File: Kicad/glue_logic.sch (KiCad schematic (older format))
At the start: 14 parts, among them U12 SN74LS273, U13 DM74AS74M, U14 DM74AS74M, U15 74AS04, U16 DM74S05M, U17 74F151A, U18 DM74AS74M, U19 74F151A, U37 DM74AS74M, U49 SN74AS258, U5 DM74S05M, U50 SN74AS258, U51 DM74AS74M, U7 DM74AS74M

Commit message: few glued wires
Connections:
- net labels added: CN4_5, D20, D22, D23, D24, U36_13, U44_1, U46_19, U6_13, U6_16, U6_34, U6_73, _BOSS, _IPL1
- wire segments 204 -> 264
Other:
- moved on the sheet: U12, U37, U5
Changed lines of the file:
@@
 L New_Library_0:DM74AS74M U37
 U 1 1 5DC69234
-P 3400 7050
-F 0 "U37" H 3567 7615 50  0000 C CNN
-F 1 "DM74AS74M" H 3567 7524 50  0000 C CNN
-F 2 "" H 3400 7050 50  0001 C CNN
-F 3 "" H 3400 7050 50  0001 C CNN
-	1    3400 7050
+P 5950 7050
+F 0 "U37" H 6117 7615 50  0000 C CNN
+F 1 "DM74AS74M" H 6117 7524 50  0000 C CNN
+F 2 "" H 5950 7050 50  0001 C CNN
+F 3 "" H 5950 7050 50  0001 C CNN
+	1    5950 7050
 	1    0    0    -1
 $EndComp
@@
 L New_Library_0:DM74S05M U5
 U 1 1 5DC6A3D2
-P 1200 7000
-F 0 "U5" H 1200 7565 50  0000 C CNN
-F 1 "DM74S05M" H 1200 7474 50  0000 C CNN
-F 2 "" H 1200 6800 50  0001 C CNN
-F 3 "" H 1200 6800 50  0001 C CNN
-	1    1200 7000
+P 2550 6700
+F 0 "U5" H 2550 7265 50  0000 C CNN
+F 1 "DM74S05M" H 2550 7174 50  0000 C CNN
+F 2 "" H 2550 6500 50  0001 C CNN
+F 3 "" H 2550 6500 50  0001 C CNN
+	1    2550 6700
 	1    0    0    -1
 $EndComp
@@
 L New_Library_0:SN74LS273 U12
 U 1 1 5DC6B7D4
-P 2250 7000
-F 0 "U12" H 2225 7665 50  0000 C CNN
-F 1 "SN74LS273" H 2225 7574 50  0000 C CNN
-F 2 "" H 2250 7250 50  0001 C CNN
-F 3 "" H 2250 7250 50  0001 C CNN
-	1    2250 7000
+P 8800 5400
+F 0 "U12" H 8775 6065 50  0000 C CNN
+F 1 "SN74LS273" H 8775 5974 50  0000 C CNN
+F 2 "" H 8800 5650 50  0001 C CNN
+F 3 "" H 8800 5650 50  0001 C CNN
+	1    8800 5400
 	1    0    0    -1
 $EndComp
@@
 U3_16
 Wire Wire Line
-	1100 5650 1800 5650
+	1100 5650 1600 5650
 Wire Wire Line
 	1800 5650 1800 5350
@@
 Wire Wire Line
 	2050 4300 2150 4300
-Wire Wire Line
-	1100 4250 2050 4250
 Text GLabel 1100 2850 0    50   Input ~ 0
 U9_10
@@
 	5400 5550 5200 5550
 Wire Wire Line
+	1950 6400 2250 6400
+Wire Wire Line
+	1100 4250 2050 4250
+Text GLabel 1100 6700 0    50   Input ~ 0
+U6_13
+Wire Wire Line
+	2250 6700 1100 6700
+Wire Wire Line
+	2100 5950 2100 6600
+Wire Wire Line
+	2100 6600 2250 6600
+Wire Wire Line
+	2100 5950 5800 5950
+Wire Wire Line
+	5800 5950 5800 2150
+Wire Wire Line
+	5800 2150 5350 2150
+Text GLabel 1100 2150 0    50   Input ~ 0
+U6_34
+Wire Wire Line
+	4550 1650 4300 1650
+Wire Wire Line
+	4300 1650 4300 1000
+Wire Wire Line
+	4300 1000 1250 1000
+Wire Wire Line
+	1250 1000 1250 2150
+Wire Wire Line
+	1250 2150 1100 2150
+Wire Wire Line
+	4550 1850 4450 1850
+Wire Wire Line
+	4450 1850 4450 1400
+$Comp
+L power:+5V #PWR?
+U 1 1 5DA035B7
+P 4450 1400
+F 0 "#PWR?" H 4450 1250 50  0001 C CNN
+F 1 "+5V" H 4465 1573 50  0000 C CNN
+F 2 "" H 4450 1400 50  0001 C CNN
+F 3 "" H 4450 1400 50  0001 C CNN
+	1    4450 1400
+	1    0    0    -1
+$EndComp
+$Comp
+L power:+5V #PWR?
+U 1 1 5DA039F0
+P 5450 1400
+F 0 "#PWR?" H 5450 1250 50  0001 C CNN
+F 1 "+5V" H 5465 1573 50  0000 C CNN
+F 2 "" H 5450 1400 50  0001 C CNN
+F 3 "" H 5450 1400 50  0001 C CNN
+	1    5450 1400
+	1    0    0    -1
+$EndComp
+Wire Wire Line
+	5350 1550 5450 1550
+Wire Wire Line
+	5450 1550 5450 1400
+Wire Wire Line
+	4650 3950 4550 3950
+Wire Wire Line
+	4550 3950 4550 3500
+Wire Wire Line
+	4550 3500 6200 3500
+Wire Wire Line
+	6200 3500 6200 2200
+Wire Wire Line
+	6200 2200 6400 2200
+Text GLabel 6400 2200 2    50   Input ~ 0
+CN4_5
+Text Label 6200 2200 0    50   ~ 0
+_RES
+Wire Wire Line
+	4650 4050 4400 4050
+Wire Wire Line
+	4400 4050 4400 5850
+Wire Wire Line
+	1900 5850 1900 4950
+Wire Wire Line
+	1900 4950 1100 4950
+Wire Wire Line
+	1900 5850 4400 5850
+Text Label 1150 4950 0    50   ~ 0
+_BOSS
+Wire Wire Line
+	5250 4350 6400 4350
+Wire Wire Line
+	5250 4250 5900 4250
+Wire Wire Line
+	5900 4250 5900 2300
+Wire Wire Line
+	5900 2300 6350 2300
+Text GLabel 6400 2300 2    50   Input ~ 0
+U36_13
+Text GLabel 6400 2400 2    50   Input ~ 0
+U44_1
+Wire Wire Line
+	6400 2400 6350 2400
+Wire Wire Line
+	6350 2400 6350 2300
+Connection ~ 6350 2300
+Wire Wire Line
+	6350 2300 6400 2300
+Wire Wire Line
+	6400 3950 6400 3850
+Wire Wire Line
+	6300 3850 6400 3850
+Connection ~ 6400 3850
+Wire Wire Line
+	2250 6800 1600 6800
+Wire Wire Line
+	1600 5650 1600 6800
+Connection ~ 1600 5650
+Wire Wire Line
+	1600 5650 1800 5650
+Wire Wire Line
+	2250 6900 1100 6900
+Text Label 1150 6900 0    50   ~ 0
+_IPL1
+Wire Wire Line
+	7800 5300 7250 5300
+Wire Wire Line
+	7800 5000 8000 5000
+Wire Wire Line
+	7800 5000 7800 5300
+Text GLabel 8000 4750 1    50   Input ~ 0
+U6_73
+Wire Wire Line
+	8000 4750 8000 5000
+Connection ~ 8000 5000
+Wire Wire Line
+	8000 5000 8450 5000
+Text GLabel 8100 4750 1    50   Input ~ 0
+U6_16
+Wire Wire Line
+	8100 4750 8100 5100
+Wire Wire Line
+	8100 5100 8450 5100
+Wire Wire Line
+	8450 5200 8200 5200
+Wire Wire Line
+	8200 5200 8200 4750
+Text GLabel 8200 4750 1    50   Input ~ 0
+U46_19
+Text Label 8200 4800 3    50   ~ 0
+D20
+Wire Wire Line
+	8450 5300 8300 5300
+Wire Wire Line
+	8300 5300 8300 4750
+Text Label 8300 4800 3    50   ~ 0
+D24
+Wire Wire Line
+	8450 5500 8000 5500
+Wire Wire Line
+	8000 5500 8000 6050
+Wire Wire Line
+	8450 5600 8100 5600
+Wire Wire Line
+	8100 5600 8100 6050
+Wire Wire Line
+	8450 5700 8200 5700
+Wire Wire Line
+	8200 5700 8200 6050
+Wire Wire Line
+	8450 5800 8300 5800
+Wire Wire Line
+	8300 5800 8300 6050
+Text Label 8100 5850 3    50   ~ 0
+D22
+Text Label 8200 5850 3    50   ~ 0
+D23
+Wire Wire Line
+	10200 4700 10350 4700
+Wire Wire Line
+	10350 4700 10350 4500
+Wire Wire Line
+	8650 3000 9250 3000
+Wire Wire Line
+	8650 1500 9250 1500
+Wire Wire Line
 	7300 1400 8000 1400
 Wire Wire Line
 	7300 2900 8000 2900
-Wire Wire Line
-	8650 3000 9250 3000
-Wire Wire Line
-	8650 1500 9250 1500
 Wire Bus Line
 	9350 700  9350 3200
@@
 	7200 700  7200 3100
 Wire Bus Line
+	9150 600  9150 3100
+Wire Bus Line
 	7450 600  7450 3000
-Wire Bus Line
-	9150 600  9150 3100
 $EndSCHEMATC

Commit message: nothing special
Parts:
- added R38, R39: 220R, symbol Device:R
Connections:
- net labels added: D16, D17, D18, D19, U11_12, U30_18, U6_58, U6_59, U6_61, U8_35
- wire segments 264 -> 295
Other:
- moved on the sheet: U37
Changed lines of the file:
@@
 L New_Library_0:DM74AS74M U37
 U 1 1 5DC69234
-P 5950 7050
-F 0 "U37" H 6117 7615 50  0000 C CNN
-F 1 "DM74AS74M" H 6117 7524 50  0000 C CNN
-F 2 "" H 5950 7050 50  0001 C CNN
-F 3 "" H 5950 7050 50  0001 C CNN
-	1    5950 7050
+P 4900 6850
+F 0 "U37" H 5067 7415 50  0000 C CNN
+F 1 "DM74AS74M" H 5067 7324 50  0000 C CNN
+F 2 "" H 4900 6850 50  0001 C CNN
+F 3 "" H 4900 6850 50  0001 C CNN
+	1    4900 6850
 	1    0    0    -1
 $EndComp
@@
 	7800 5300 7250 5300
 Wire Wire Line
-	7800 5000 8000 5000
+	7800 5000 7900 5000
 Wire Wire Line
 	7800 5000 7800 5300
-Text GLabel 8000 4750 1    50   Input ~ 0
+Text GLabel 7900 4750 1    50   Input ~ 0
 U6_73
 Wire Wire Line
-	8000 4750 8000 5000
-Connection ~ 8000 5000
-Wire Wire Line
-	8000 5000 8450 5000
-Text GLabel 8100 4750 1    50   Input ~ 0
+	7900 4750 7900 5000
+Connection ~ 7900 5000
+Wire Wire Line
+	7900 5000 8450 5000
+Text GLabel 8300 4750 1    50   Input ~ 0
 U6_16
 Wire Wire Line
-	8100 4750 8100 5100
-Wire Wire Line
-	8100 5100 8450 5100
+	8300 4750 8300 5100
+Wire Wire Line
+	8300 5100 8450 5100
 Wire Wire Line
 	8450 5200 8200 5200
@@
 D20
 Wire Wire Line
-	8450 5300 8300 5300
-Wire Wire Line
-	8300 5300 8300 4750
-Text Label 8300 4800 3    50   ~ 0
+	8450 5300 8100 5300
+Wire Wire Line
+	8100 5300 8100 4750
+Text Label 8100 4800 3    50   ~ 0
 D24
 Wire Wire Line
 	8450 5500 8000 5500
 Wire Wire Line
-	8000 5500 8000 6050
+	8000 5500 8000 5950
 Wire Wire Line
 	8450 5600 8100 5600
@@
 	8450 5800 8300 5800
 Wire Wire Line
-	8300 5800 8300 6050
+	8300 5800 8300 5950
 Text Label 8100 5850 3    50   ~ 0
 D22
@@
 D23
 Wire Wire Line
-	10200 4700 10350 4700
-Wire Wire Line
-	10350 4700 10350 4500
+	9100 5700 9350 5700
+Wire Wire Line
+	9350 5700 9350 6050
+Text Label 9450 5850 3    50   ~ 0
+D17
+Wire Wire Line
+	9100 5600 9450 5600
+Wire Wire Line
+	9450 5600 9450 6050
+Text Label 9350 5850 3    50   ~ 0
+D18
+Wire Wire Line
+	9100 5200 9450 5200
+Wire Wire Line
+	9450 5200 9450 4750
+Text Label 9450 4800 3    50   ~ 0
+D19
+Wire Wire Line
+	9100 5300 9550 5300
+Wire Wire Line
+	9550 5300 9550 4750
+Text Label 9550 4800 3    50   ~ 0
+D16
+Wire Wire Line
+	8450 5400 8000 5400
+Wire Wire Line
+	8000 5400 8000 4750
+Wire Wire Line
+	9100 5900 9200 5900
+Wire Wire Line
+	9200 5900 9200 6250
+Wire Wire Line
+	7800 6250 7800 5500
+Wire Wire Line
+	7800 5500 7250 5500
+Text GLabel 8050 6350 2    50   Input ~ 0
+U30_18
+Wire Wire Line
+	7800 6250 7900 6250
+Wire Wire Line
+	8050 6350 7900 6350
+Wire Wire Line
+	7900 6350 7900 6250
+Connection ~ 7900 6250
+Wire Wire Line
+	7900 6250 9200 6250
+Text GLabel 8000 4750 1    50   Input ~ 0
+U6_61
+Text Label 8000 4800 3    50   ~ 0
+D24
+Text GLabel 8000 5950 3    50   Input ~ 0
+U6_58
+Text Label 8000 5800 3    50   ~ 0
+D22
+Text Label 8300 5850 3    50   ~ 0
+D23
+Text GLabel 8300 5950 3    50   Input ~ 0
+U6_59
+$Comp
+L power:+5V #PWR?
+U 1 1 5DD59290
+P 4450 6400
+F 0 "#PWR?" H 4450 6250 50  0001 C CNN
+F 1 "+5V" H 4465 6573 50  0000 C CNN
+F 2 "" H 4450 6400 50  0001 C CNN
+F 3 "" H 4450 6400 50  0001 C CNN
+	1    4450 6400
+	1    0    0    -1
+$EndComp
+Wire Wire Line
+	5300 6550 5350 6550
+Wire Wire Line
+	5350 6550 5350 6400
+Wire Wire Line
+	5350 6400 4450 6400
+Text GLabel 1100 7150 0    50   Input ~ 0
+U8_35
+Wire Wire Line
+	1100 7150 3450 7150
+Wire Wire Line
+	4450 6400 4450 6550
+Wire Wire Line
+	4450 6550 4500 6550
+Connection ~ 4450 6400
+Wire Wire Line
+	4500 6750 4000 6750
+Wire Wire Line
+	4000 6750 4000 7150
+Wire Wire Line
+	5300 6850 5600 6850
+Wire Wire Line
+	5600 6850 5600 7450
+Wire Wire Line
+	5600 7450 4000 7450
+Wire Wire Line
+	4000 7450 4000 7150
+Connection ~ 4000 7150
+$Comp
+L Device:R R38
+U 1 1 5E5CC419
+P 3450 7000
+F 0 "R38" H 3520 7046 50  0000 L CNN
+F 1 "220R" H 3520 6955 50  0000 L CNN
+F 2 "" V 3380 7000 50  0001 C CNN
+F 3 "~" H 3450 7000 50  0001 C CNN
+	1    3450 7000
+	1    0    0    -1
+$EndComp
+Connection ~ 3450 7150
+Wire Wire Line
+	3450 7150 4000 7150
+$Comp
+L Device:R R39
+U 1 1 5E5CCBD0
+P 3450 7300
+F 0 "R39" H 3520 7346 50  0000 L CNN
+F 1 "220R" H 3520 7255 50  0000 L CNN
+F 2 "" V 3380 7300 50  0001 C CNN
+F 3 "~" H 3450 7300 50  0001 C CNN
+	1    3450 7300
+	1    0    0    -1
+$EndComp
+$Comp
+L power:+5V #PWR?
+U 1 1 5E5CD0AB
+P 3450 6850
+F 0 "#PWR?" H 3450 6700 50  0001 C CNN
+F 1 "+5V" H 3465 7023 50  0000 C CNN
+F 2 "" H 3450 6850 50  0001 C CNN
+F 3 "" H 3450 6850 50  0001 C CNN
+	1    3450 6850
+	1    0    0    -1
+$EndComp
+$Comp
+L power:GND #PWR?
+U 1 1 5E5CD473
+P 3450 7450
+F 0 "#PWR?" H 3450 7200 50  0001 C CNN
+F 1 "GND" H 3455 7277 50  0000 C CNN
+F 2 "" H 3450 7450 50  0001 C CNN
+F 3 "" H 3450 7450 50  0001 C CNN
+	1    3450 7450
+	1    0    0    -1
+$EndComp
+Wire Wire Line
+	4500 6650 4000 6650
+Wire Wire Line
+	4000 6650 4000 6600
 Wire Wire Line
 	8650 3000 9250 3000
@@
 Wire Bus Line
 	7450 600  7450 3000
+Text GLabel 4000 6600 1    50   Input ~ 0
+U11_12
 $EndSCHEMATC

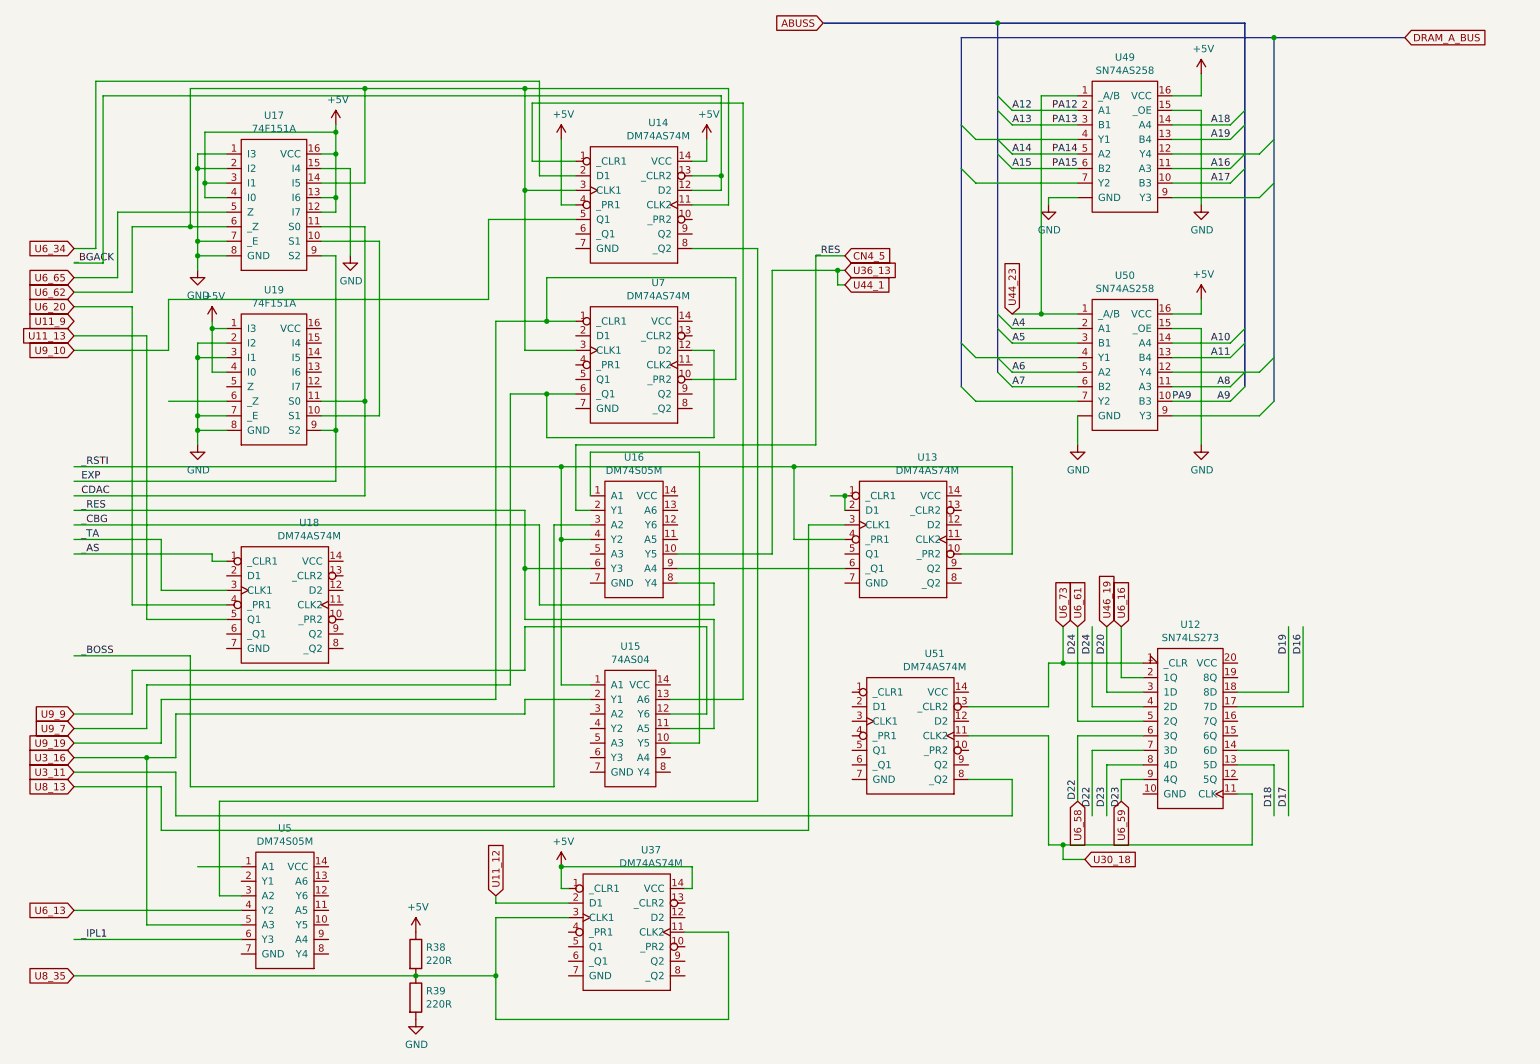
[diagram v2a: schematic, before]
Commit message: some dram schematics
dram section, data and address bus
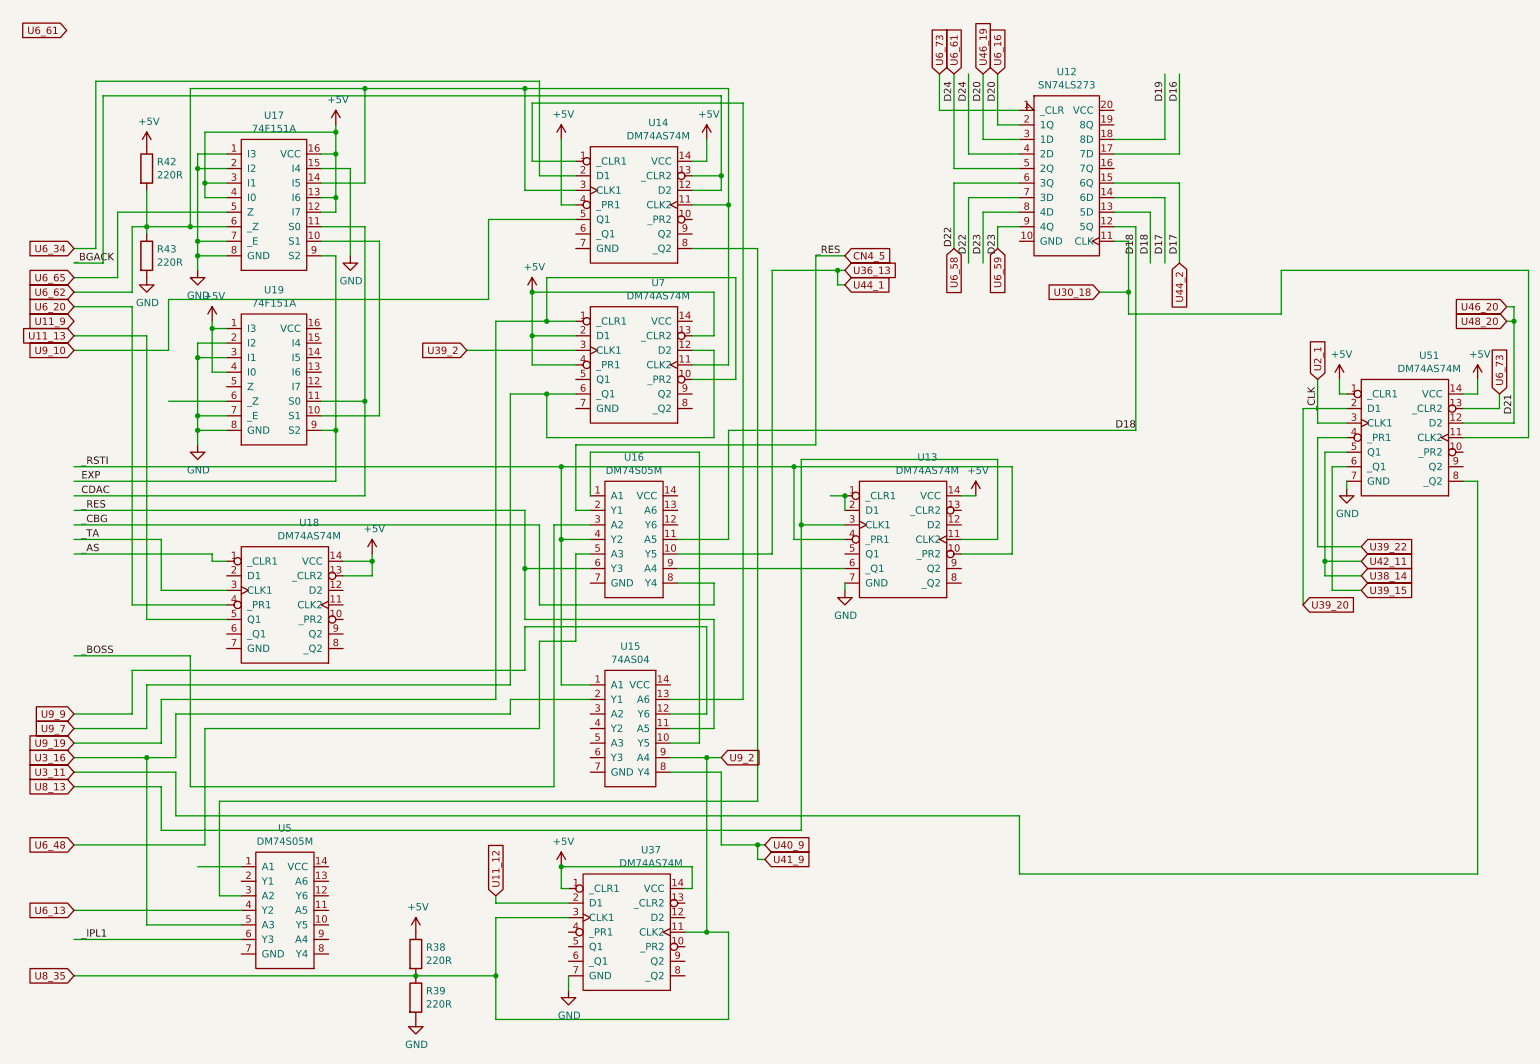
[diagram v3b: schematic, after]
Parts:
- removed U49, U50: SN74AS258, symbol New_Library_0:SN74AS258
- added R42, R43: 220R, symbol Device:R
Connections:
- net labels added: D21, U2_1, U38_14, U39_15, U39_2, U39_20, U39_22, U40_9, U41_9, U42_11, U44_2, U46_20, U48_20, U6_48, U9_2, _CLK
- net labels removed: A10, A11, A12, A13, A14, A15, A16, A17, A18, A19, A4, A5, A6, A7, A8, A9, ABUSS, DRAM_A_BUS, PA12, PA13, PA14, PA15, PA9, U44_23
- wire segments 295 -> 329
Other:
- moved on the sheet: U12, U51

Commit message: Some more work on dram
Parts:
- added RP9_1: 1K, symbol Device:R
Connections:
- net labels removed: U46_19
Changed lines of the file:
@@
 	1900 2000 1900 1050
-Wire Wire Line
-	1900 1050 3100 1050
 Wire Wire Line
 	4200 1050 4200 1750
@@
 	2800 1600 3000 1600
 Wire Wire Line
-	3000 1600 3000 2200
+	3000 1600 3000 1700
 $Comp
 L power:GND #PWR?
@@
 $EndComp
 Wire Wire Line
-	3100 1050 3100 1700
-Wire Wire Line
-	3100 1700 2800 1700
-Connection ~ 3100 1050
-Wire Wire Line
-	3100 1050 4200 1050
-Wire Wire Line
 	2800 1800 2900 1800
 Wire Wire Line
@@
 	4550 3950 4550 3500
 Wire Wire Line
-	4550 3500 6200 3500
-Wire Wire Line
-	6200 3500 6200 2200
-Wire Wire Line
-	6200 2200 6400 2200
+	4550 3500 6100 3500
+Wire Wire Line
+	6100 3500 6100 2200
+Wire Wire Line
+	6100 2200 6400 2200
 Text GLabel 6400 2200 2    50   Input ~ 0
 CN4_5
-Text Label 6200 2200 0    50   ~ 0
+Text Label 6150 2200 0    50   ~ 0
 _RES
 Wire Wire Line
@@
 Wire Wire Line
 	7350 1400 7350 950
-Text GLabel 7350 950  1    50   Input ~ 0
-U46_19
 Text Label 7350 1000 3    50   ~ 0
 D20
@@
 Text Label 7450 1000 3    50   ~ 0
 D20
+$Comp
+L power:+5V #PWR?
+U 1 1 6071AF2A
+P 3200 1700
+F 0 "#PWR?" H 3200 1550 50  0001 C CNN
+F 1 "+5V" H 3215 1873 50  0000 C CNN
+F 2 "" H 3200 1700 50  0001 C CNN
+F 3 "" H 3200 1700 50  0001 C CNN
+	1    3200 1700
+	1    0    0    -1
+$EndComp
+$Comp
+L Device:R RP9_1
+U 1 1 6071C90B
+P 3200 1850
+F 0 "RP9_1" H 3270 1896 50  0000 L CNN
+F 1 "1K" H 3270 1805 50  0000 L CNN
+F 2 "" V 3130 1850 50  0001 C CNN
+F 3 "~" H 3200 1850 50  0001 C CNN
+	1    3200 1850
+	1    0    0    -1
+$EndComp
+Wire Wire Line
+	3200 2000 3200 2100
+Connection ~ 3200 2100
+Wire Wire Line
+	1900 1050 4200 1050
+Wire Wire Line
+	2800 1700 3000 1700
+Connection ~ 3000 1700
+Wire Wire Line
+	3000 1700 3000 2200
+Text Label 6150 2300 0    50   ~ 0
+D18
 $EndSCHEMATC
